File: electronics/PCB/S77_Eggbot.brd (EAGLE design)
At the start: 70 x 70 mm, 21 parts, among them U1 CR_LM2596, U2 S2_MINI, U3 CARRIER_A4988, U4 CARRIER_A4988, X1 PWR, X2 B6B-PH, X3 B6B-PH

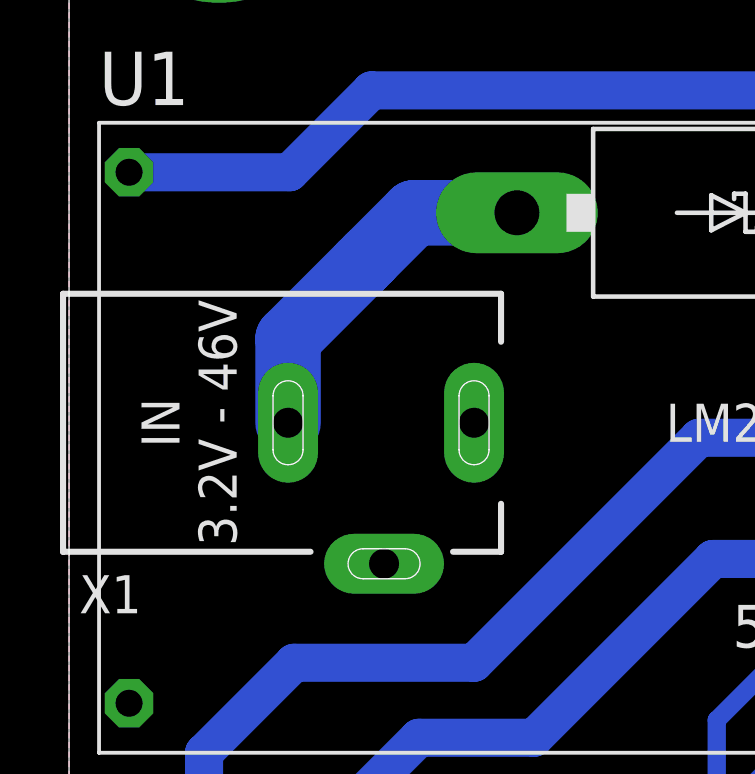
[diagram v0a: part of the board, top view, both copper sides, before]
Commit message: Fix: swap Pin 1 and 2 on barrel jack X1
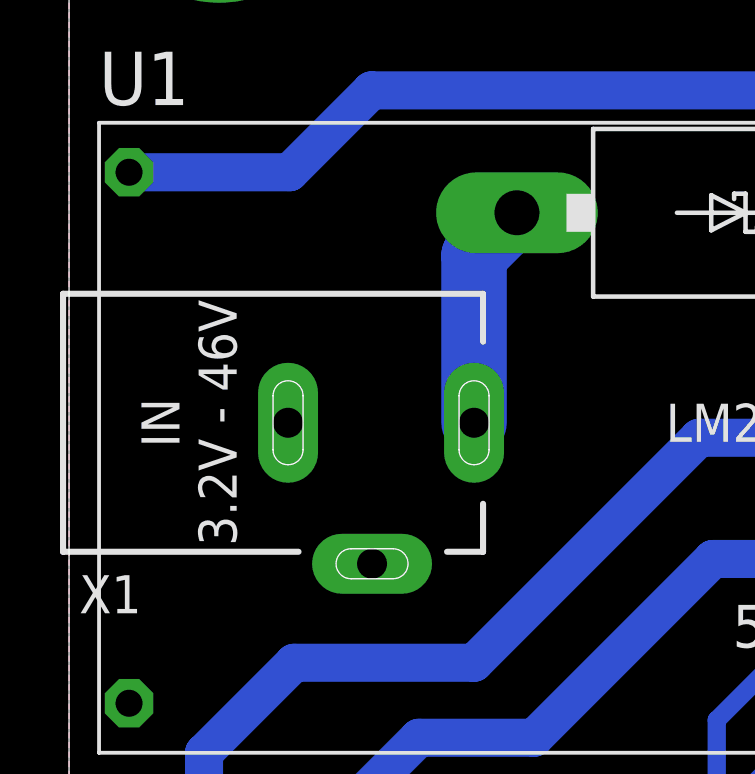
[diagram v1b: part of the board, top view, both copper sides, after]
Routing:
- net N$3: track 12.2 -> 7.59 mm
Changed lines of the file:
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@@
 <contactref element="D1" pad="A"/>
 <contactref element="X1" pad="1"/>
-<wire x1="7.3" y1="47" x2="7.3" y2="49.8" width="2.1844" layer="16"/>
-<wire x1="7.3" y1="49.8" x2="9.75" y2="52.25" width="2.1844" layer="16"/>
-<wire x1="9.75" y1="52.25" x2="10" y2="52.5" width="2.1844" layer="16"/>
-<wire x1="14.93" y1="54" x2="11.5" y2="54" width="2.1844" layer="16"/>
-<wire x1="11.5" y1="54" x2="10" y2="52.5" width="2.1844" layer="16"/>
+<wire x1="13.5" y1="47" x2="13.5" y2="52.57" width="2.1844" layer="16"/>
+<wire x1="13.5" y1="52.57" x2="14.93" y2="54" width="2.1844" layer="16"/>
 </signal>
 <signal name="+5V">

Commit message: PCB: update date
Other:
- board text added: "eggbot77 section77.de 09.02.2024"
- board text removed: "eggbot77 section77.de 25.01.2024"
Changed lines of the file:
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@@
 <text x="26.73" y="40.98" size="2.54" layer="26" font="vector" rot="MR180" align="center">eggbot77
 section77.de
-25.01.2024</text>
+09.02.2024</text>
 <text x="39.215" y="41.285" size="1.4224" layer="21" font="vector" rot="R180" align="center-left">ATTENTION:
 Trim output to
